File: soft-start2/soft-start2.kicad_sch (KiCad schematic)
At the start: 33 parts, among them J3 Conn_01x01_Pin, J4 Conn_01x01_Pin, K1 Relay_SPST-NO, K2 Relay_SPST-NO, M1 Motor_DC, Q1 IRFB3004PbF, Q2 IRFB3004PbF, SW2 SW_SPST_Temperature, U1 TLC555xD, U2 IRS10752LPbF

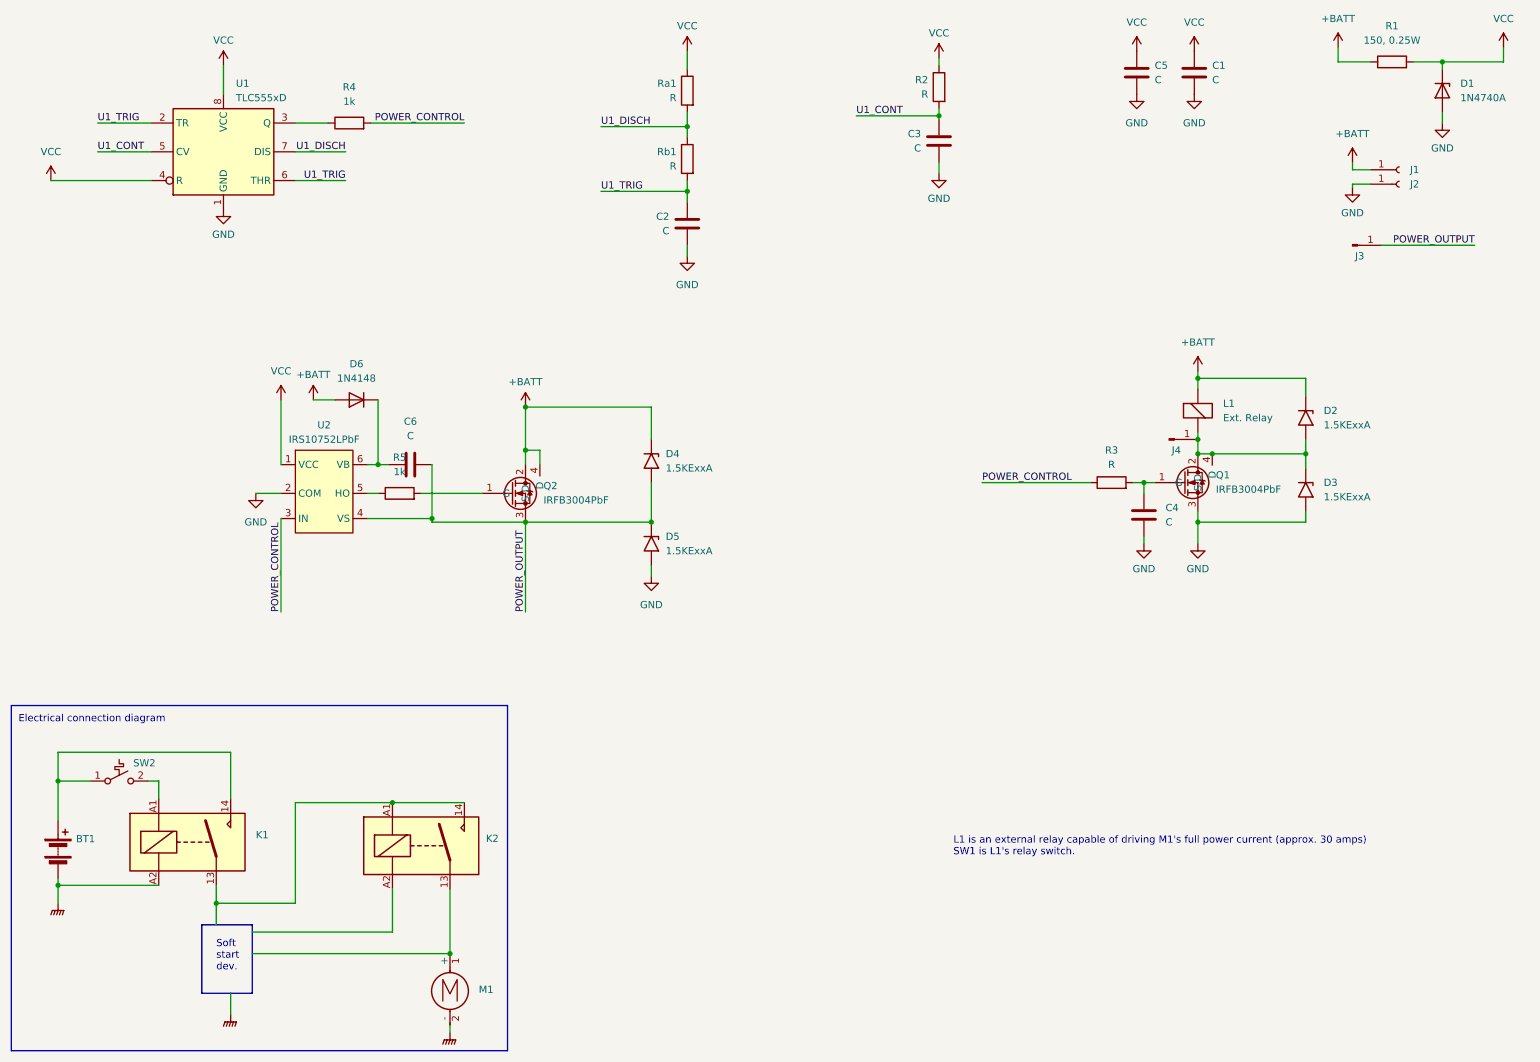
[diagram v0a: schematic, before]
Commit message: [soft-start] Add calculus file. Add integrating and comparator schematic for turning on full-power.
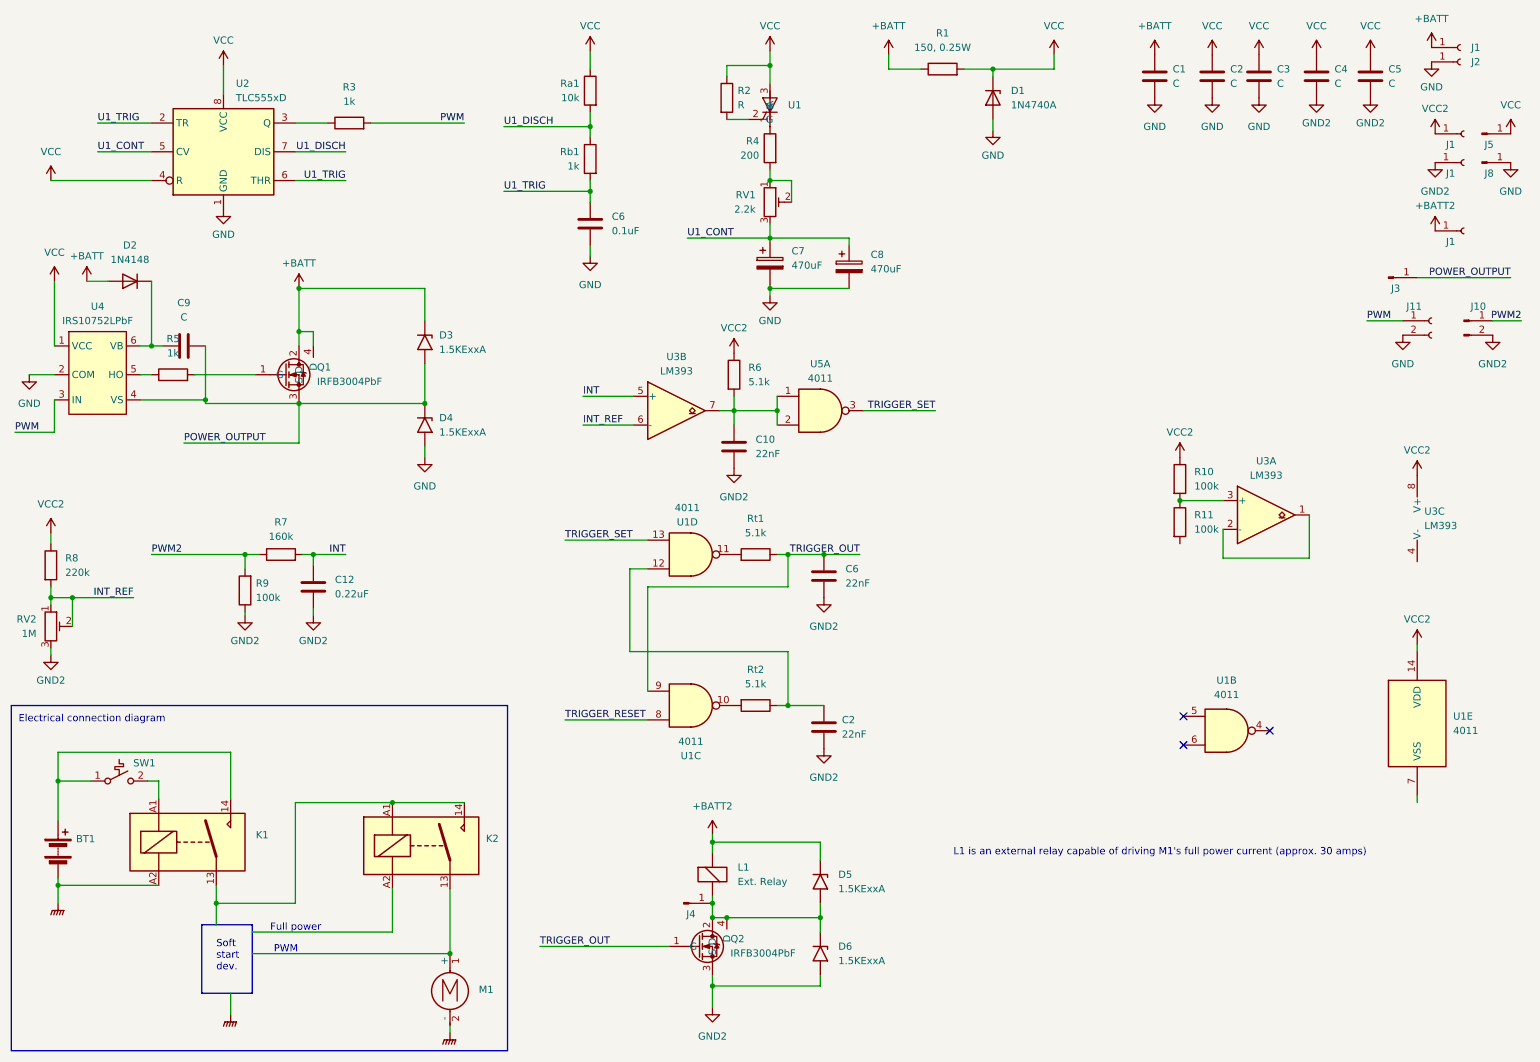
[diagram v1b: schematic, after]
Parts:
- removed C3: C, Capacitor_THT:C_Disc_D5.0mm_W2.5mm_P5.00mm, symbol Device:C
- added C1, C2, C5: C, Capacitor_THT:C_Disc_D5.0mm_W2.5mm_P5.00mm, symbol Device:C
- added C10: 22nF, Capacitor_THT:C_Disc_D5.0mm_W2.5mm_P5.00mm, symbol Device:C
- added C2, C6: 22nF, Capacitor_THT:C_Disc_D6.0mm_W4.4mm_P5.00mm, symbol Device:C
- added C7, C8: 470uF, Capacitor_THT:CP_Radial_D8.0mm_P3.80mm, symbol Device:C_Polarized
- added J1 (x3): ~, Connector_Wire:SolderWire-2.5sqmm_1x01_D2.4mm_OD3.6mm, symbol Connector:Conn_01x01_Socket
- added J10: Conn_01x02_Pin, Connector_Wire:SolderWire-0.5sqmm_1x02_P4.6mm_D0.9mm_OD2.1mm, symbol Connector:Conn_01x02_Pin
- added J11: Conn_01x02_Socket, Connector_Wire:SolderWire-0.5sqmm_1x02_P4.6mm_D0.9mm_OD2.1mm, symbol Connector:Conn_01x02_Socket
- added J5, J8: Conn_01x01_Pin, Connector_Wire:SolderWire-2.5sqmm_1x01_D2.4mm_OD3.6mm, symbol Connector:Conn_01x01_Pin
- added R10, R11, R9: 100k, Resistor_THT:R_Axial_DIN0207_L6.3mm_D2.5mm_P5.08mm_Vertical, symbol Device:R
- added R2: R, Resistor_THT:R_Axial_DIN0207_L6.3mm_D2.5mm_P5.08mm_Vertical, symbol Device:R
- added R6: 5.1k, Resistor_THT:R_Axial_DIN0207_L6.3mm_D2.5mm_P5.08mm_Vertical, symbol Device:R
- added R8: 220k, Resistor_THT:R_Axial_DIN0207_L6.3mm_D2.5mm_P5.08mm_Vertical, symbol Device:R
- added RV1: 2.2k, Potentiometer_THT:Potentiometer_Bourns_3296W_Vertical, symbol Device:R_Potentiometer_Trim
- added RV2: 1M, Potentiometer_THT:Potentiometer_Bourns_3296W_Vertical, symbol Device:R_Potentiometer_Trim
- added Rt1, Rt2: 5.1k, Resistor_THT:R_Axial_DIN0204_L3.6mm_D1.6mm_P5.08mm_Horizontal, symbol Device:R
- added U1, U5: 4011, Package_DIP:DIP-14_W7.62mm_Socket_LongPads, symbol 4xxx:4011
- added U3: LM393, Package_DIP:DIP-8_W7.62mm_Socket_LongPads, symbol Comparator:LM393
- C12: renamed from C4; value C -> 0.22uF
- C6: renamed from C2; value C -> 0.1uF
- Q1: renamed from Q2; footprint Package_TO_SOT_SMD:TO-263-2 -> LIB:TO-220-3-4_Horizontal_TabDown
- R4: renamed from R2; value R -> 200
- R7: renamed from R3; value R -> 160k
- Ra1: value R -> 10k
- Rb1: value R -> 1k
- renumbered C5 to C3, C1 to C4, C6 to C9, D6 to D2, D4 to D3, D5 to D4, D2 to D5, D3 to D6, Q1 to Q2, R4 to R3, SW2 to SW1, U1 to U2, U2 to U4
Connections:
- net +BATT: now also C1.1; no longer D5.1 (A1), L1.1 (-)
- net GND: now also C1.2, C2.2, C7.2, C8.2, J11.2 (Pin_2), J8.1 (Pin_1); no longer C12.2, C4.2, D6.2 (A2), Q2.3 (S)
- net U1_CONT: now also C7.1, C8.1, RV1.3; no longer R4.2
- net VCC: now also C2.1, C5.1, J5.1 (Pin_1), R2.1, U1.3 (A); no longer R4.1
- net INT: now reaches C12.1, R7.2
- net INT: now also U3.5 (+); no longer Q2.1 (G)
- net POWER_CONTROL renamed PWM
- net PWM: now also J11.1 (Pin_1); no longer R7.1
- new net: C10.1, R6.2, U3.7, U5.1, U5.2
- new net: Rt1.2, U1.11
- new net: C2.1, Rt2.1, U1.12
- new net: R2.2, U1.2 (G)
- new net: Rt2.2, U1.10
- new net: R4.1, U1.1 (K)
- new net: R4.2, RV1.1, RV1.2
- new net: R10.2, R11.1, U3.3 (+)
- new net: U3.1, U3.2 (-)
- new net +BATT2: D5.1 (A1), J1.1 (Pin_1), L1.1 (-)
- new net GND2: C10.2, C12.2, C2.2, C4.2, C5.2, C6.2, D6.2 (A2), J1.1 (Pin_1), J10.2 (Pin_2), Q2.3 (S), R9.1, RV2.3
- new net INT_REF: R8.2, RV2.1, RV2.2, U3.6 (-)
- new net PWM2: J10.1 (Pin_1), R7.1, R9.2
- new net TRIGGER_OUT: C6.1, Q2.1 (G), Rt1.1, U1.9
- new net TRIGGER_RESET: U1.8
- new net TRIGGER_SET: U1.13, U5.3
- new net VCC2: J1.1 (Pin_1), R10.1, R6.1, R8.1, U1.14 (VDD), U3.8 (V+)
- no-connect marks 0 -> 3
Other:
- note added: "Full power"
- note added: "L1 is an external relay capable of driving M1's full power current (approx. 30 amps)"
- note added: "PWM"
- note removed: "L1 is an external relay capable of driving M1's full power current (approx. 30 amps) SW1 is L1's relay switch."
- moved on the sheet: C12, C3, C4, C6, C9, D1, D2, D3, D4, D5, D6, J1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

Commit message: [soft-start] Change comparator. Start PCB.
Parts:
- removed R10, R11: 100k, Resistor_THT:R_Axial_DIN0207_L6.3mm_D2.5mm_P5.08mm_Vertical, symbol Device:R
- removed U3: LM393, Package_DIP:DIP-8_W7.62mm_Socket_LongPads, symbol Comparator:LM393
- added U3: TS391ILT, Package_TO_SOT_SMD:SOT-23-5_HandSoldering, symbol comparator:TS391ILT
- D2: footprint Diode_THT:D_DO-35_SOD27_P7.62mm_Horizontal -> Diode_THT:D_DO-35_SOD27_P5.08mm_Vertical_KathodeUp
- Q1: footprint LIB:TO-220-3-4_Horizontal_TabDown -> Package_TO_SOT_SMD:TO-263-2
- R3, R4: footprint Resistor_THT:R_Axial_DIN0207_L6.3mm_D2.5mm_P5.08mm_Vertical -> Resistor_THT:R_Axial_DIN0207_L6.3mm_D2.5mm_P7.62mm_Horizontal
- Rb1: footprint Resistor_THT:R_Axial_DIN0207_L6.3mm_D2.5mm_P5.08mm_Vertical -> Resistor_THT:R_Axial_DIN0207_L6.3mm_D2.5mm_P10.16mm_Horizontal
- U1: value ~ -> P0102BL
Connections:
- net GND2: now also U1.7 (VSS), U3.2 (VCC-)
- net INT: now also U3.4 (+)
- net INT_REF: now also U3.3 (-)
- net VCC: no longer C4.1, C5.1
- net VCC2: now also C4.1, C5.1, U3.5 (VCC+)
- net at C10.1, R6.2, U5.1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: now also U3.1
